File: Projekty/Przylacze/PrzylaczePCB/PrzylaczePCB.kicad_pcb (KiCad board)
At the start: 4 copper layers, 99.1 x 114.8 mm, 134 parts, among them J1 Conn_02x20_Odd_Even, J2 USB_B, J3 Conn_01x06, J4 Conn_02x04_Odd_Even, J5 Screw_Terminal_01x06, M3 MountingHole_3.2mm_M3, Q1 BC547, Q10 BC557, Q11 2N3904, Q12 2N7002, Q2 BC547, Q3 BC547, Q4 BC557, Q5 2N3904, Q6 BC557, Q7 BC557, Q8 BC547, Q9 BC557, SW1 SW_Push, SW2 SW_SPDT, SW3 SW_SPDT, SW4 SW_SPDT, SW5 SW_SPDT, SW6 SW_SPDT, SW7 SW_SPDT, SW8 SW_SPDT, SW9 SW_SPDT, U1 MCP2561-E-P, U2 ATSAM4S2AA-AU, U3 MCP2515-xSO, U4 TJA1055T_3_C,518, U5 MAX3485, U6 74AHC1G04, U7 LDL1117S33R, U8 DI78M05UAB, U9 74AHC1G04, Y1 20MHz

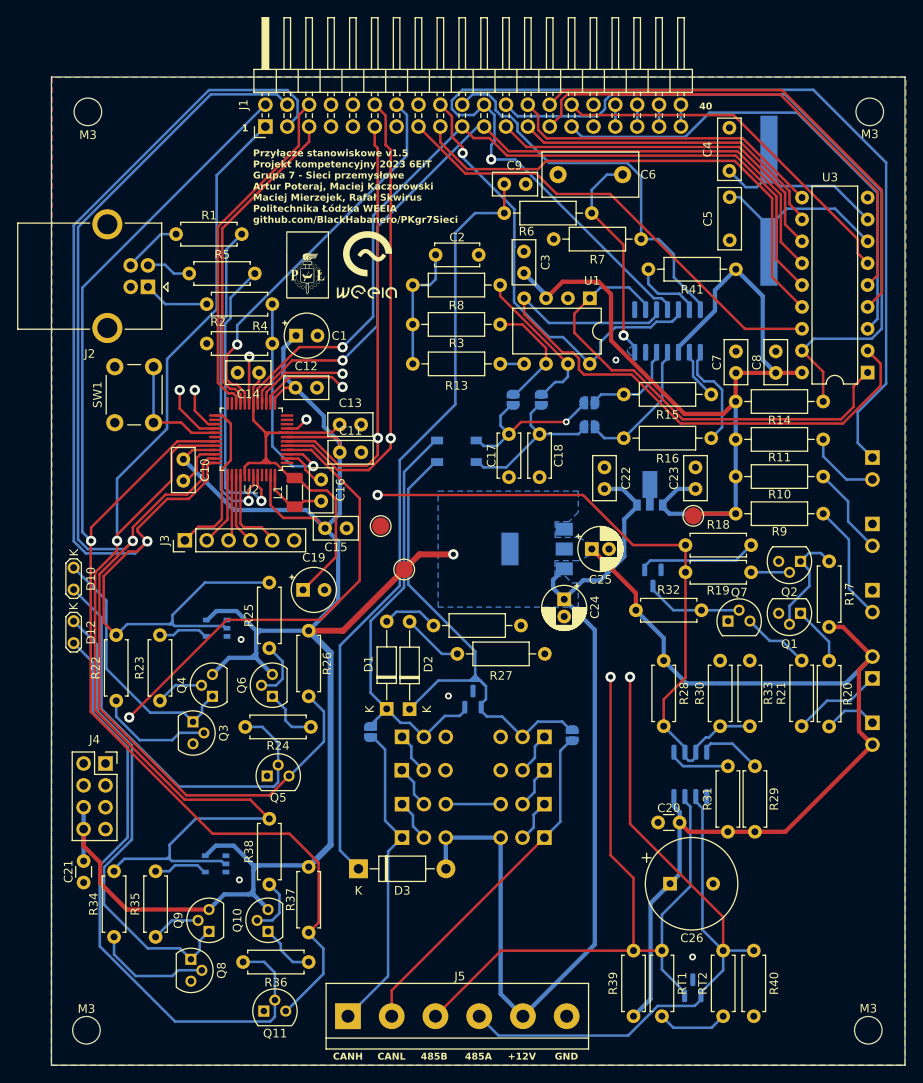
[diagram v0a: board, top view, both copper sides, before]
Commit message: Przyłącze - projekt PCB v1.5.2
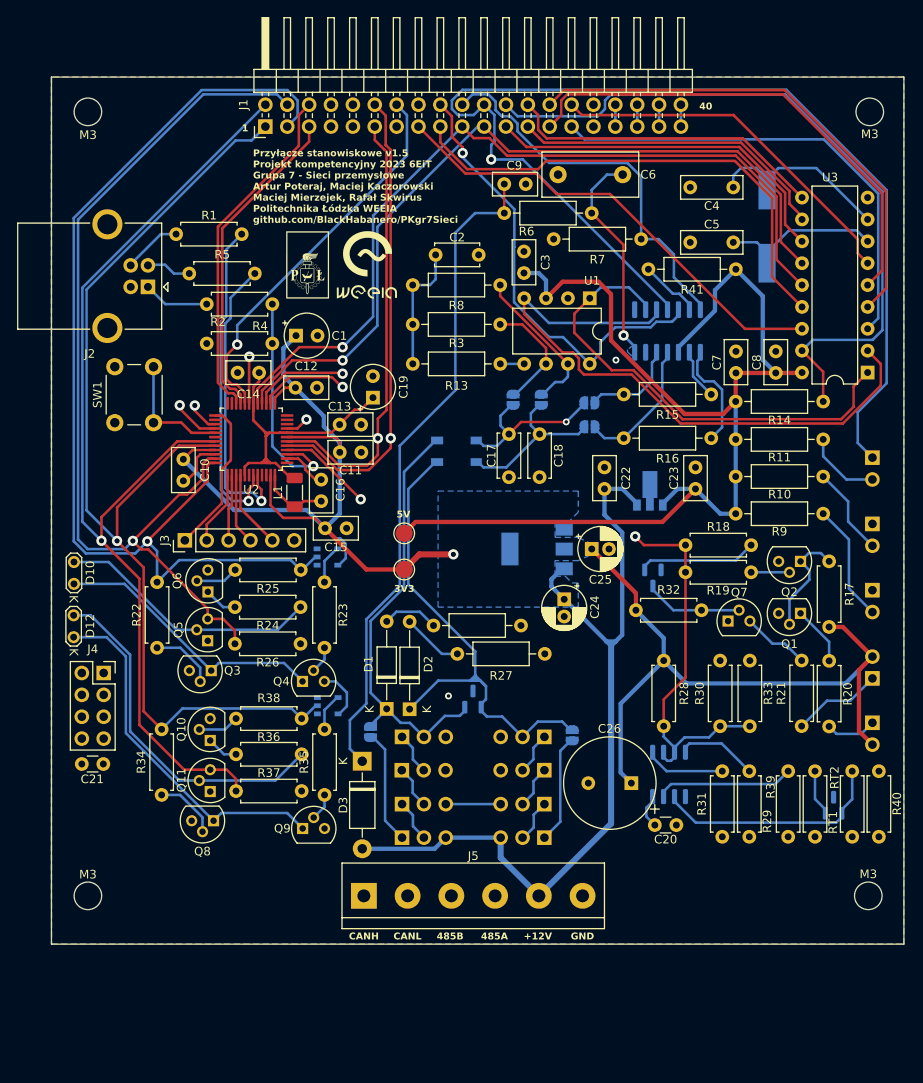
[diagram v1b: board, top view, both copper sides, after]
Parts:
- removed the REF** at (78.4, 134.5)
- Y1: footprint Crystal:Crystal_SMD_HC49-SD_HandSoldering -> Crystal:Crystal_SMD_HC49-SD
- moved REF** 33.6 mm to (81.1, 135.3)
- moved R39 27.5 mm to (125.7, 170.6)
- moved RT1 27.4 mm to (128.8, 162.9)
- moved D11 26.8 mm to (131.0, 166.9)
- moved Q11 26.2 mm to (58.6, 165.3), turned to 90 degrees
- moved RT2 25.7 mm to (133.1, 170.6)
- moved R35 25.6 mm to (71.8, 165.7)
- moved R36 25.6 mm to (61.6, 161.0), turned to 0 degrees
- moved R40 25.4 mm to (136.2, 162.9)
- moved C19 23.8 mm to (77.5, 119.6), turned to 90 degrees
- moved Q10 23.2 mm to (58.6, 159.4)
- moved U9 22.5 mm to (72.2, 155.3), turned to 90 degrees
- moved R23 20.1 mm to (71.8, 148.6)
- moved R38 19.6 mm to (61.6, 156.8), turned to 0 degrees
- moved R37 18.5 mm to (61.6, 165.3), turned to 0 degrees
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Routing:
- net OPTO_R1: track 150.0 -> 108.1 mm
- net OPTO_R2: track 154.1 -> 118.4 mm
- net Net-(D12-A): track 72.7 -> 40.9 mm
- net +5V: track 104.3 -> 134.0 mm
- net +3.3V: track 332.1 -> 304.3 mm
- net OPTO_SW2: track 148.2 -> 121.4 mm
- net OPTO_SW1: track 140.1 -> 121.7 mm
- net Net-(D10-A): track 48.8 -> 30.7 mm
- net CS0: track 120.2 -> 105.1 mm
- net CANH: track 142.1 -> 127.3 mm
- net +12V: track 108.9 -> 95.2 mm
- net Net-(D3-K): track 90.3 -> 77.0 mm
- net Net-(U2-VDDOUT): track 47.3 -> 34.7 mm
- net Net-(D12-K): track 53.9 -> 41.8 mm
- net MISO: track 162.4 -> 151.1 mm
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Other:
- board size 99.1 x 114.8 mm -> 99 x 100.7 mm
- board text added: "3V3"
- board text added: "5V"

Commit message: Przyłącze - projekt PCB v1.6
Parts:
- removed Q10, Q9: BC557, Package_TO_SOT_THT:TO-92L
- removed Q11: 2N3904, Package_TO_SOT_THT:TO-92L
- removed Q8: BC547, Package_TO_SOT_THT:TO-92L
- removed R35, R38: 1k, Resistor_THT:R_Axial_DIN0207_L6.3mm_D2.5mm_P7.62mm_Horizontal
- removed R36: 360, Resistor_THT:R_Axial_DIN0207_L6.3mm_D2.5mm_P7.62mm_Horizontal
- removed R37: 470k, Resistor_THT:R_Axial_DIN0207_L6.3mm_D2.5mm_P7.62mm_Horizontal
- added RV1: 20k, Potentiometer_THT:Potentiometer_Bourns_3006P_Horizontal, F.Cu at (58.0, 167.6)
- added RV2: 20k, Potentiometer_THT:Potentiometer_Bourns_3006P_Horizontal, F.Cu at (65.5, 167.6)
- added U10: 74AHC1G04, PrzylaczeFootprintLibrary:Nexperia-SOT753-10_2018-0-0, B.Cu at (53.5, 143.6)
- added U11: 74AHC1G04, PrzylaczeFootprintLibrary:Nexperia-SOT753-10_2018-0-0, B.Cu at (53.5, 148.5)
- Q3: value BC547 -> 2N7002; footprint Package_TO_SOT_THT:TO-92L -> Package_TO_SOT_SMD:SOT-23; moved to B.Cu
- Q4: value BC557 -> 2N3904
- Q6: value BC557 -> 2N7002; footprint Package_TO_SOT_THT:TO-92L -> Package_TO_SOT_SMD:SOT-23; moved to B.Cu
- R22, R23, R25: value 1k -> R; footprint Resistor_THT:R_Axial_DIN0207_L6.3mm_D2.5mm_P7.62mm_Horizontal -> Resistor_THT:R_Axial_DIN0207_L6.3mm_D2.5mm_P10.16mm_Horizontal
- R24: value 360 -> R; footprint Resistor_THT:R_Axial_DIN0207_L6.3mm_D2.5mm_P7.62mm_Horizontal -> Resistor_THT:R_Axial_DIN0207_L6.3mm_D2.5mm_P10.16mm_Horizontal
- R26: value 470k -> 10k; footprint Resistor_THT:R_Axial_DIN0207_L6.3mm_D2.5mm_P7.62mm_Horizontal -> Resistor_THT:R_Axial_DIN0207_L6.3mm_D2.5mm_P10.16mm_Horizontal
- R34: value 1k -> 10k; footprint Resistor_THT:R_Axial_DIN0207_L6.3mm_D2.5mm_P7.62mm_Horizontal -> Resistor_THT:R_Axial_DIN0207_L6.3mm_D2.5mm_P10.16mm_Horizontal
- U6: value 74AHC1G04 -> NE5532P; footprint PrzylaczeFootprintLibrary:Nexperia-SOT753-10_2018-0-0 -> PrzylaczeFootprintLibrary:Texas_Instruments-NE5532P; moved to F.Cu
- U9: value 74AHC1G04 -> TLV3202AID; footprint PrzylaczeFootprintLibrary:Nexperia-SOT753-10_2018-0-0 -> PrzylaczeFootprintLibrary:TLV3202AID
- moved R24 26.7 mm to (52.5, 169.1), turned to 180 degrees
- moved U6 19.8 mm to (62.9, 155.5), turned to -90 degrees
- moved R22 18.5 mm to (69.0, 140.4), turned to 180 degrees
- moved Q5 18.3 mm to (51.3, 164.7)
- moved R25 13.7 mm to (71.4, 149.0), turned to -90 degrees
- moved R34 12.4 mm to (42.4, 172.2), turned to 0 degrees
- moved U9 12.3 mm to (62.8, 163.3), turned to 0 degrees
- moved R26 11.5 mm to (50.0, 149.3), turned to -90 degrees
- moved R23 10.6 mm to (61.8, 145.1), turned to 0 degrees
- moved Q4 10.1 mm to (69.9, 162.6), turned to -90 degrees
- moved Q3 7.45 mm to (57.9, 143.9), turned to 0 degrees
- moved Q6 6.66 mm to (57.9, 148.8), turned to 0 degrees
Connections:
- D10 pad 1: Net-(D10-K) -> GND
- D12 pad 1: Net-(D12-K) -> GND
- J1 pad 1: OPTO_SW2 -> OPTO2_TX
- J1 pad 2: OPTO_R2 -> OPTO2_RX
- J1 pad 3: OPTO_SW1 -> OPTO1_TX
- J1 pad 4: OPTO_R1 -> OPTO1_RX
- Q3 pad 1: Net-(D10-K) -> OPTO1_NOT_TX
- Q3 pad 2: Net-(Q3-B) -> Net-(D10-A)
- Q3 pad 3: GND -> Net-(Q3-D)
- Q4 pad 1: Net-(D10-K) -> Net-(Q4-E)
- Q5 pad 1: GND -> Net-(Q5-E)
- Q5 pad 2: Net-(D10-A) -> Net-(Q5-B)
- Q5 pad 3: OPTO_R1 -> +3.3V
- Q6 pad 1: Net-(Q6-C) -> OPTO2_NOT_TX
- Q6 pad 2: Net-(Q6-B) -> Net-(D12-A)
- Q6 pad 3: +3.3V -> Net-(Q6-D)
- R22 pad 1: Net-(Q3-B) -> OPTO1_OPAMP
- R22 pad 2: OPTO_SW1 -> Net-(Q3-D)
- R23 pad 1: Net-(Q4-B) -> Net-(Q6-D)
- R23 pad 2: Net-(R23-Pad2) -> OPTO2_OPAMP
- R24 pad 1: Net-(Q6-C) -> Net-(Q5-E)
- R24 pad 2: Net-(D10-A) -> Net-(D12-A)
- R25 pad 1: Net-(Q6-B) -> Net-(D10-A)
- R25 pad 2: OPTO_SW1 -> Net-(Q4-E)
- R26 pad 1: OPTO_R1 -> OPTO2_TX
- R26 pad 2: +3.3V -> Net-(Q5-B)
- R34 pad 1: Net-(Q8-B) -> OPTO1_TX
- R34 pad 2: OPTO_SW2 -> Net-(Q4-B)
- U2 pad 31: OPTO_R2 -> OPTO2_RX
- U2 pad 32: OPTO_SW2 -> OPTO2_TX
- U2 pad 35: OPTO_R1 -> OPTO1_RX
- U2 pad 36: OPTO_SW1 -> OPTO1_TX
- U6 pad 1: (no net) -> OPTO2_OPAMP
- U6 pad 2: OPTO_SW1 -> Net-(Q6-D)
- U6 pad 4: Net-(R23-Pad2) -> +3.3V
- U6 pad 5: +3.3V -> GND
- U9 pad 1: (no net) -> OPTO1_RX
- U9 pad 2: OPTO_SW2 -> OPTO1_POT
- U9 pad 3: GND -> OPTO1_OPAMP
- U9 pad 4: Net-(R35-Pad2) -> GND
- U9 pad 5: +3.3V -> OPTO2_OPAMP
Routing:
- net OPTO1_TX: track 0.00 -> 139.6 mm, vias 0 -> 1
- net OPTO1_RX: track 0.00 -> 126.6 mm, vias 0 -> 2
- net OPTO_SW1: track 121.7 -> 0.00 mm, vias 1 -> 0
- net OPTO_SW2: track 121.4 -> 0.00 mm, vias 1 -> 0
- net OPTO2_RX: track 0.00 -> 118.6 mm, vias 0 -> 2
- net OPTO_R2: track 118.4 -> 0.00 mm, vias 1 -> 0
- net OPTO_R1: track 108.1 -> 0.00 mm, vias 1 -> 0
- net OPTO2_TX: track 0.00 -> 95.4 mm, vias 0 -> 1
- net Net-(D12-K): track 41.8 -> 0.00 mm
- net Net-(D10-K): track 32.0 -> 0.00 mm
- net OPTO1_OPAMP: track 0.00 -> 26.8 mm
- net Net-(Q3-D): track 0.00 -> 26.0 mm
- net OPTO2_OPAMP: track 0.00 -> 20.6 mm
- net Net-(Q4-B): track 3.17 -> 23.4 mm
- net OPTO2_POT: track 0.00 -> 14.7 mm
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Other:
- board text added: "Przyłącze stanowiskowe v1.6 Projekt kompetencyjny 2023 6EiT Grupa 7 - Sieci przemysłowe Artur Poteraj, Maciej Kaczorowski Maciej Mierzejek, Rafał Skwirus Politechnika Łódzka WEEIA github.com/BlackHabanero/PKgr7Sieci"
- board text removed: "Przyłącze stanowiskowe v1.5 Projekt kompetencyjny 2023 6EiT Grupa 7 - Sieci przemysłowe Artur Poteraj, Maciej Kaczorowski Maciej Mierzejek, Rafał Skwirus Politechnika Łódzka WEEIA github.com/BlackHabanero/PKgr7Sieci"

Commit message: PeCeBe wersja Final Omega Prime Ultimate Fatality
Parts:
- added R35: 600, Resistor_THT:R_Axial_DIN0207_L6.3mm_D2.5mm_P10.16mm_Horizontal, F.Cu at (62.2, 156.8)
- added R36: 600, Resistor_THT:R_Axial_DIN0207_L6.3mm_D2.5mm_P10.16mm_Horizontal, F.Cu at (62.2, 161.3)
- Q3, Q6: value 2N7002 -> BC547; footprint Package_TO_SOT_SMD:SOT-23 -> Package_TO_SOT_THT:TO-92_Inline; moved to F.Cu
- R22, R23: value R -> 1M
- moved U10 28.6 mm to (72.5, 165.1)
- moved R34 28.2 mm to (62.2, 152.2)
- moved R24 28.0 mm to (65.3, 144.2)
- moved Q5 26.4 mm to (69.3, 145.5), turned to 0 degrees
- moved R22 23.9 mm to (59.9, 162.6)
- moved U11 22.6 mm to (68.9, 165.1)
- moved Q4 21.8 mm to (69.3, 140.7), turned to 0 degrees
- moved R25 18.6 mm to (55.2, 139.7), turned to 0 degrees
- moved R23 13.0 mm to (49.6, 149.4)
- moved U9 12.3 mm to (68.2, 174.3), turned to 90 degrees
- moved R26 12.2 mm to (62.2, 149.0), turned to 0 degrees
- moved Q3 8.52 mm to (51.0, 138.9), turned to -90 degrees
- moved U6 7.65 mm to (55.2, 156.0)
- moved Q6 6.60 mm to (52.5, 145.0), turned to 180 degrees
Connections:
- Q3 pad 1: OPTO1_NOT_TX -> Net-(D10-A)
- Q3 pad 2: Net-(D10-A) -> Net-(Q3-B)
- Q6 pad 1: OPTO2_NOT_TX -> Net-(D12-A)
- Q6 pad 2: Net-(D12-A) -> Net-(Q6-B)
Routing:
- net Net-(D12-A): track 45.1 -> 13.6 mm, vias 1 -> 0
- net Net-(Q6-B): track 0.00 -> 23.1 mm
- net OPTO1_RX: track 126.6 -> 149.6 mm
- net Net-(Q3-B): track 0.00 -> 22.7 mm
- net OPTO2_TX: track 95.4 -> 118.1 mm
- net Net-(D10-A): track 34.2 -> 12.7 mm, vias 1 -> 0
- net OPTO2_RX: track 118.6 -> 133.0 mm
- net Net-(Q4-B): track 23.4 -> 14.6 mm
- net OPTO2_POT: track 14.7 -> 5.93 mm
- net OPTO1_NOT_TX: track 2.62 -> 10.5 mm
- net OPTO2_OPAMP: track 20.6 -> 26.7 mm
- net GND: track 10.7 -> 16.4 mm
- net OPTO2_NOT_TX: track 2.55 -> 5.98 mm
- net RADIO_IRQ: track 56.1 -> 59.4 mm
- net OPTO1_OPAMP: track 26.8 -> 29.6 mm
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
